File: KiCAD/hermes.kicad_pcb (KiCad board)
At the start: 2 copper layers, 32.8 x 53.6 mm, 10 parts, among them U1 MPU-6500, U2 XIAO-RP2040-DIP

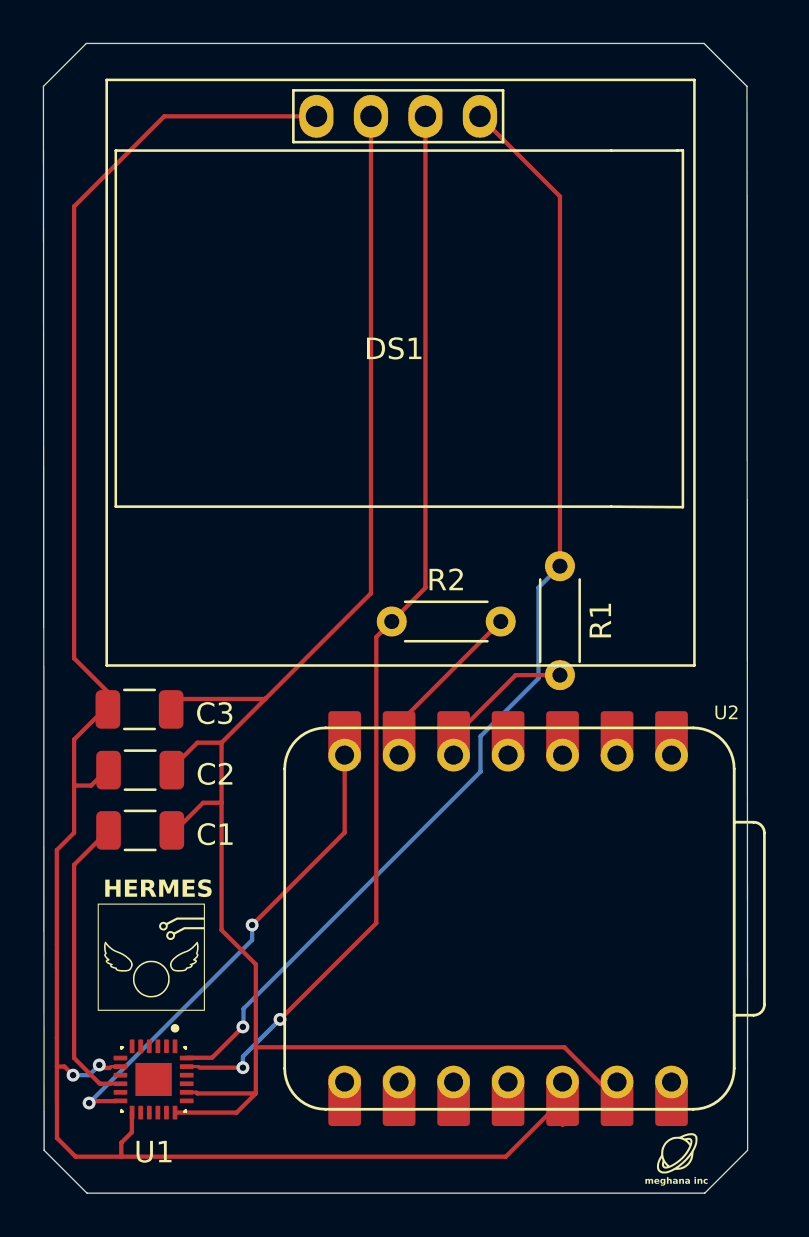
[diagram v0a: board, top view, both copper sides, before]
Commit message: fixed pullups
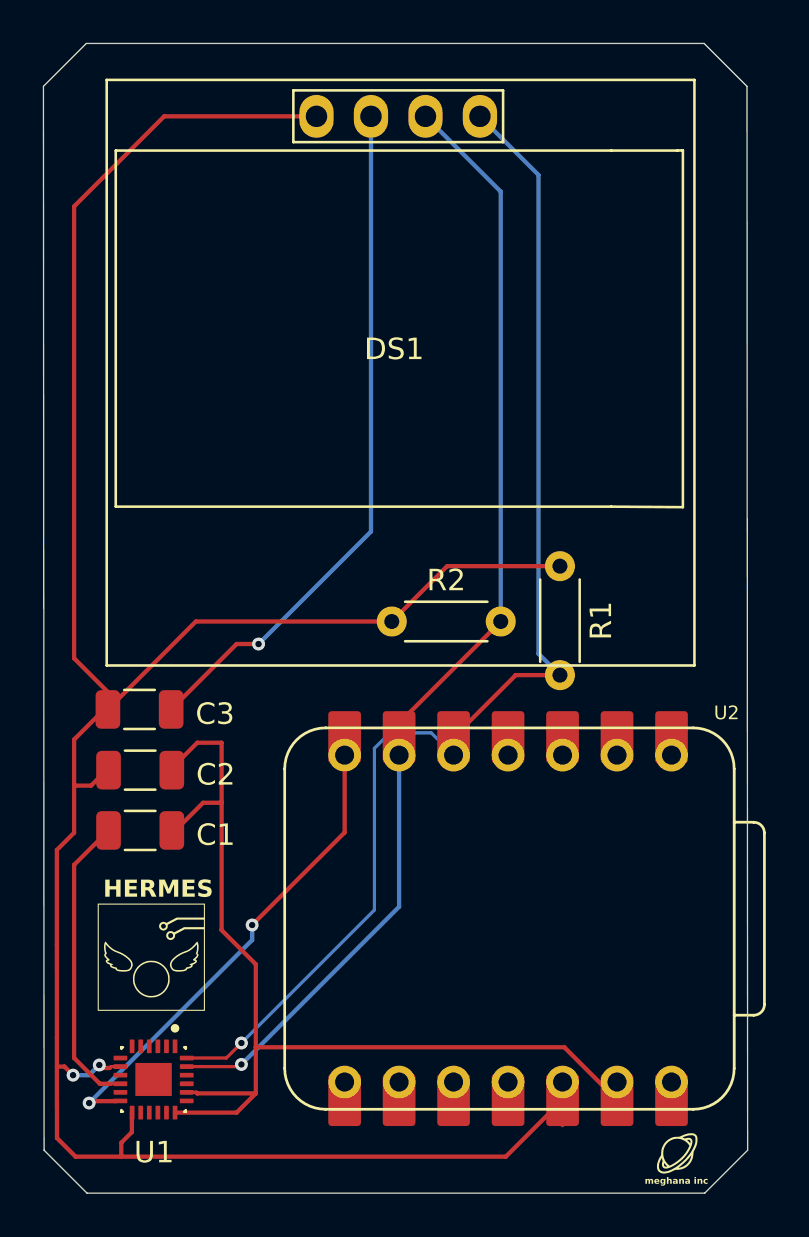
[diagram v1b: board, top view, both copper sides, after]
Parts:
- C1, C3: value C -> 0.1 µF
- R1, R2: value R -> 4.7k
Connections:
- R1 pad 1: SDA -> 3V3
- R1 pad 2: Net-(U2-GPIO6/SDA) -> SDA
- R2 pad 1: SCL -> 3V3
- R2 pad 2: Net-(U2-GPIO7/SCL) -> SCL
- U2 pad 5: Net-(U2-GPIO6/SDA) -> SDA
- U2 pad 6: Net-(U2-GPIO7/SCL) -> SCL
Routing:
- net 3V3: track 93.6 -> 117.4 mm
- net Net-(U2-GPIO7/SCL): track 7.36 -> 0.00 mm
- net Net-(U2-GPIO6/SDA): track 6.16 -> 0.00 mm
- net GND: track 83.0 -> 79.0 mm, vias 0 -> 1
- net SDA: track 53.3 -> 57.3 mm
- net SCL: track 50.5 -> 53.3 mm, vias 2 -> 1
